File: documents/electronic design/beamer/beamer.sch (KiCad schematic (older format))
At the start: 23 parts, among them P1 CONN_01X20, P2 CONN_01X20, T1 2N7002K, T10 2N7002K, T2 2N7002K, T3 2N7002K, T4 2N7002K, T5 2N7002K, T6 2N7002K, T7 2N7002K, T8 2N7002K, T9 2N7002K, U1 NRF24L01-BRKOUT

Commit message: update schematics and pcb projects
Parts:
- T1, T10, T2, T3, T4, T5, T6, T7, T8, T9: footprint SOT23 -> 2N7002K:SOT23
- U1: footprint NRF24L01-BKKOUT -> se8r01_smd:SE8R01_SMD
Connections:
- net IR_PIN_1: now also P1.8 (P8); no longer P2.8 (P8)
- net IR_PIN_2: now also P1.9 (P9); no longer P2.7 (P7)
- net IR_PIN_3: now also P1.10 (P10); no longer P1.11 (P11)
- net IR_PIN_4: now also P1.11 (P11); no longer P1.12 (P12)
- net IR_PIN_5: now also P1.12 (P12); no longer P1.13 (P13)
- net IR_PIN_6: now also P1.13 (P13); no longer P1.14 (P14)
- net IR_PIN_7: now also P1.14 (P14); no longer P1.15 (P15)
- net IR_PIN_8: now also P1.15 (P15); no longer P1.16 (P16)
- net IR_PIN_ID: now also P1.16 (P16); no longer P1.1 (P1)
- no-connect marks 23 -> 22
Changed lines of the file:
@@
 EESchema Schematic File Version 2
+LIBS:power
+LIBS:device
+LIBS:transistors
+LIBS:conn
+LIBS:linear
+LIBS:regul
+LIBS:74xx
+LIBS:cmos4000
+LIBS:adc-dac
+LIBS:memory
+LIBS:xilinx
+LIBS:microcontrollers
+LIBS:dsp
+LIBS:microchip
+LIBS:analog_switches
+LIBS:motorola
+LIBS:texas
+LIBS:intel
+LIBS:audio
+LIBS:interface
+LIBS:digital-audio
+LIBS:philips
+LIBS:display
+LIBS:cypress
+LIBS:siliconi
+LIBS:opto
+LIBS:atmel
+LIBS:contrib
+LIBS:valves
+LIBS:2N7002K
 LIBS:NRF24L01-BRKOUT
-LIBS:ir_beamer-cache
+LIBS:conn_R
+LIBS:beamer-cache
 EELAYER 25 0
 EELAYER END
@@
 F 0 "T1" H 1150 2150 50  0000 L CNN
 F 1 "2N7002K" H 1000 2050 50  0000 L CNN
-F 2 "SOT23" H 1350 1900 50  0001 L CNN
+F 2 "2N7002K:SOT23" H 1350 1900 50  0001 L CNN
 F 3 "" H 1350 1900 60  0000 C CNN
 	1    1350 1900
@@
 F 0 "T4" H 2650 3050 50  0000 L CNN
 F 1 "2N7002K" H 2500 2950 50  0000 L CNN
-F 2 "SOT23" H 2850 2800 50  0001 L CNN
+F 2 "2N7002K:SOT23" H 2850 2800 50  0001 L CNN
 F 3 "" H 2850 2800 60  0000 C CNN
 	1    2850 2800
@@
 F 0 "T2" H 1750 2150 50  0000 L CNN
 F 1 "2N7002K" H 1600 2050 50  0000 L CNN
-F 2 "SOT23" H 1950 1900 50  0001 L CNN
+F 2 "2N7002K:SOT23" H 1950 1900 50  0001 L CNN
 F 3 "" H 1950 1900 60  0000 C CNN
 	1    1950 1900
@@
 F 0 "T3" H 2350 2150 50  0000 L CNN
 F 1 "2N7002K" H 2200 2050 50  0000 L CNN
-F 2 "SOT23" H 2550 1900 50  0001 L CNN
+F 2 "2N7002K:SOT23" H 2550 1900 50  0001 L CNN
 F 3 "" H 2550 1900 60  0000 C CNN
 	1    2550 1900
@@
 F 0 "T5" H 2950 2150 50  0000 L CNN
 F 1 "2N7002K" H 2800 2050 50  0000 L CNN
-F 2 "SOT23" H 3150 1900 50  0001 L CNN
+F 2 "2N7002K:SOT23" H 3150 1900 50  0001 L CNN
 F 3 "" H 3150 1900 60  0000 C CNN
 	1    3150 1900
@@
 F 0 "T6" H 3550 2150 50  0000 L CNN
 F 1 "2N7002K" H 3400 2050 50  0000 L CNN
-F 2 "SOT23" H 3750 1900 50  0001 L CNN
+F 2 "2N7002K:SOT23" H 3750 1900 50  0001 L CNN
 F 3 "" H 3750 1900 60  0000 C CNN
 	1    3750 1900
@@
 F 0 "T7" H 4150 2150 50  0000 L CNN
 F 1 "2N7002K" H 4000 2050 50  0000 L CNN
-F 2 "SOT23" H 4350 1900 50  0001 L CNN
+F 2 "2N7002K:SOT23" H 4350 1900 50  0001 L CNN
 F 3 "" H 4350 1900 60  0000 C CNN
 	1    4350 1900
@@
 F 0 "T8" H 4750 2150 50  0000 L CNN
 F 1 "2N7002K" H 4600 2050 50  0000 L CNN
-F 2 "SOT23" H 4950 1900 50  0001 L CNN
+F 2 "2N7002K:SOT23" H 4950 1900 50  0001 L CNN
 F 3 "" H 4950 1900 60  0000 C CNN
 	1    4950 1900
@@
 F 0 "T9" H 5350 2150 50  0000 L CNN
 F 1 "2N7002K" H 5200 2050 50  0000 L CNN
-F 2 "SOT23" H 5550 1900 50  0001 L CNN
+F 2 "2N7002K:SOT23" H 5550 1900 50  0001 L CNN
 F 3 "" H 5550 1900 60  0000 C CNN
 	1    5550 1900
@@
 F 0 "T10" H 6600 2150 50  0000 L CNN
 F 1 "2N7002K" H 6450 2050 50  0000 L CNN
-F 2 "SOT23" H 6800 1900 50  0001 L CNN
+F 2 "2N7002K:SOT23" H 6800 1900 50  0001 L CNN
 F 3 "" H 6800 1900 60  0000 C CNN
 	1    6800 1900
@@
 Text GLabel 4450 5300 0    60   Input ~ 0
 NRF_IRQ1
-Text GLabel 4450 4300 0    60   Input ~ 0
+Text GLabel 2900 4300 2    60   Input ~ 0
 IR_PIN_1
-Text GLabel 4450 4200 0    60   Input ~ 0
+Text GLabel 2900 4400 2    60   Input ~ 0
 IR_PIN_2
+Text GLabel 2900 4500 2    60   Input ~ 0
+IR_PIN_3
 Text GLabel 2900 4600 2    60   Input ~ 0
-IR_PIN_3
+IR_PIN_4
 Text GLabel 2900 4700 2    60   Input ~ 0
-IR_PIN_4
+IR_PIN_5
 Text GLabel 2900 4800 2    60   Input ~ 0
-IR_PIN_5
+IR_PIN_6
 Text GLabel 2900 4900 2    60   Input ~ 0
-IR_PIN_6
+IR_PIN_7
 Text GLabel 2900 5000 2    60   Input ~ 0
-IR_PIN_7
+IR_PIN_8
 Text GLabel 2900 5100 2    60   Input ~ 0
-IR_PIN_8
-Text GLabel 2900 3600 2    60   Input ~ 0
 IR_PIN_ID
 NoConn ~ 2800 5500
 NoConn ~ 2800 5400
 NoConn ~ 2800 5300
-NoConn ~ 2800 4500
-NoConn ~ 2800 4400
-NoConn ~ 2800 4300
 NoConn ~ 2800 4200
 NoConn ~ 2800 4100
@@
 Text GLabel 2900 5200 2    60   Input ~ 0
 PWM_38K
-NoConn ~ 4500 3650
 $Comp
 L GND #PWR05
@@
 	2800 5200 2900 5200
 Wire Wire Line
-	2800 3600 2900 3600
-Wire Wire Line
 	4050 3450 4500 3450
 Wire Wire Line
@@
 $Comp
 L NRF24L01-BRKOUT U1
-U 1 1 5713BCFC
+U 1 1 5713E8BE
 P 9200 1850
 F 0 "U1" H 8800 2450 50  0000 L CNN
 F 1 "NRF24L01-BRKOUT" H 9200 1250 50  0000 L CNN
-F 2 "NRF24L01-BKKOUT" H 9200 1850 50  0001 L CNN
+F 2 "se8r01_smd:SE8R01_SMD" H 9200 1850 50  0001 L CNN
 F 3 "" H 9200 1850 60  0000 C CNN
 	1    9200 1850
 	1    0    0    -1
 $EndComp
+Wire Wire Line
+	2800 4400 2900 4400
+Wire Wire Line
+	2800 4500 2900 4500
+NoConn ~ 4450 4300
+NoConn ~ 4450 4200
+Wire Wire Line
+	2800 4300 2900 4300
+NoConn ~ 2800 3600
 $EndSCHEMATC

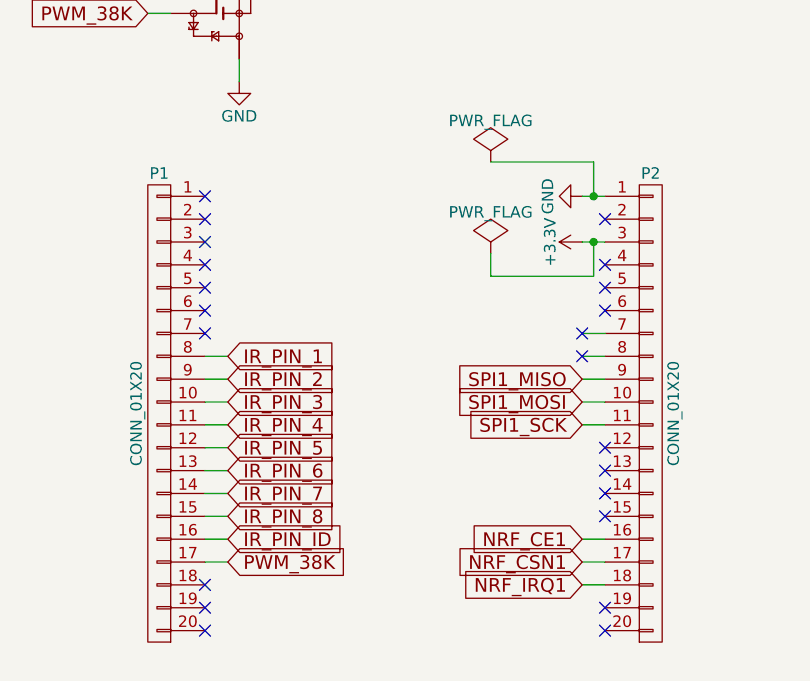
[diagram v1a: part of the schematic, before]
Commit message: finish pcb for beamer (prototype v1)
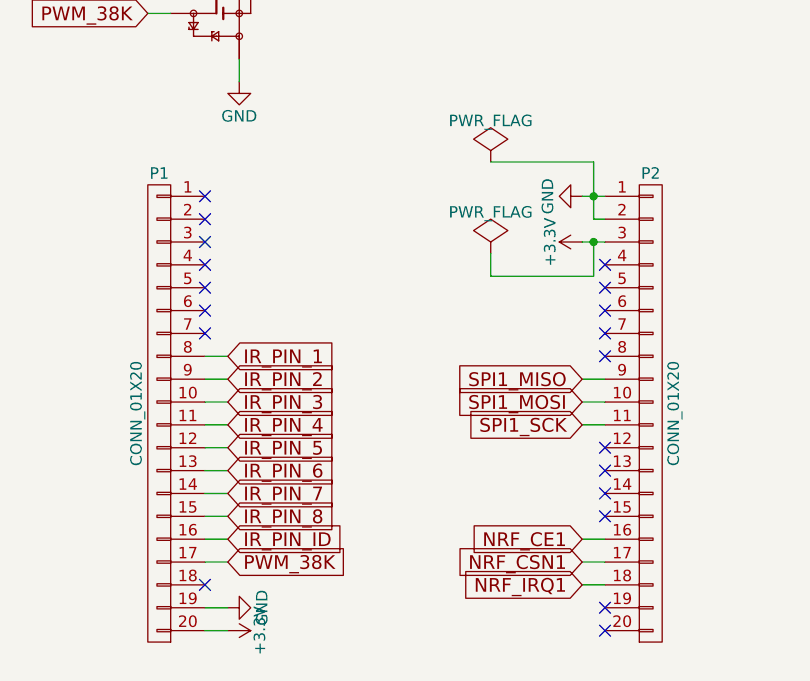
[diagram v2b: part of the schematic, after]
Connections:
- net +3V3: now also P1.20 (P20)
- net GND: now also P1.19 (P19), P2.2 (P2)
- no-connect marks 22 -> 19
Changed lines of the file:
@@
 Text GLabel 2900 5100 2    60   Input ~ 0
 IR_PIN_ID
-NoConn ~ 2800 5500
-NoConn ~ 2800 5400
 NoConn ~ 2800 5300
 NoConn ~ 2800 4200
@@
 NoConn ~ 4550 4000
 NoConn ~ 4550 3900
-NoConn ~ 4550 3700
 $Comp
 L GND #PWR03
@@
 	4450 5300 4550 5300
 Wire Wire Line
-	4450 4200 4550 4200
-Wire Wire Line
-	4450 4300 4550 4300
-Wire Wire Line
 	2800 4600 2900 4600
 Wire Wire Line
@@
 	4050 3450 4500 3450
 Wire Wire Line
-	4500 3450 4500 3600
+	4500 3450 4500 3700
 Connection ~ 4500 3600
 Wire Wire Line
@@
 Wire Wire Line
 	2800 4500 2900 4500
-NoConn ~ 4450 4300
-NoConn ~ 4450 4200
+NoConn ~ 4550 4300
+NoConn ~ 4550 4200
 Wire Wire Line
 	2800 4300 2900 4300
 NoConn ~ 2800 3600
+$Comp
+L +3.3V #PWR09
+U 1 1 57153B7B
+P 2900 5500
+F 0 "#PWR09" H 2900 5350 50  0001 C CNN
+F 1 "+3.3V" H 2900 5640 50  0000 C CNN
+F 2 "" H 2900 5500 50  0000 C CNN
+F 3 "" H 2900 5500 50  0000 C CNN
+	1    2900 5500
+	0    1    1    0
+$EndComp
+$Comp
+L GND #PWR010
+U 1 1 57153C2F
+P 2900 5400
+F 0 "#PWR010" H 2900 5150 50  0001 C CNN
+F 1 "GND" H 2900 5250 50  0000 C CNN
+F 2 "" H 2900 5400 50  0000 C CNN
+F 3 "" H 2900 5400 50  0000 C CNN
+	1    2900 5400
+	0    -1   -1   0
+$EndComp
+Wire Wire Line
+	2800 5500 2900 5500
+Wire Wire Line
+	2800 5400 2900 5400
+Wire Wire Line
+	4500 3700 4550 3700
 $EndSCHEMATC

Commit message: add capacitor to pcb
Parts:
- added C1: C, symbol C
- T1, T10, T2, T3, T4, T5, T6, T7, T8, T9: footprint 2N7002K:SOT23 -> sot23_modified:SOT23Mod
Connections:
- net +3V3: now also C1.2
- net GND: now also C1.1

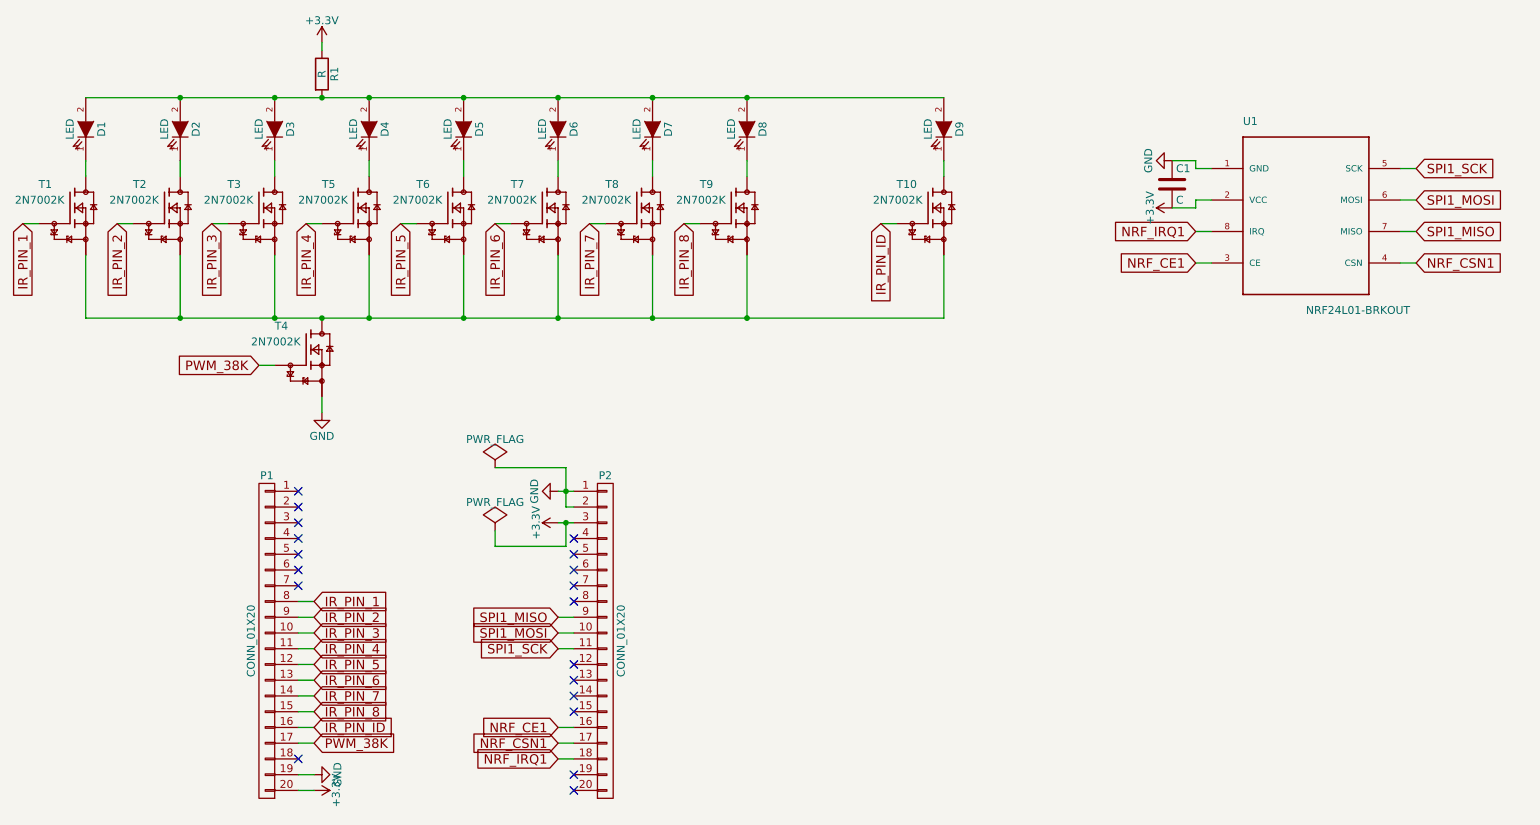
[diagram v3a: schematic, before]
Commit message: add library for shift register, update gitignore
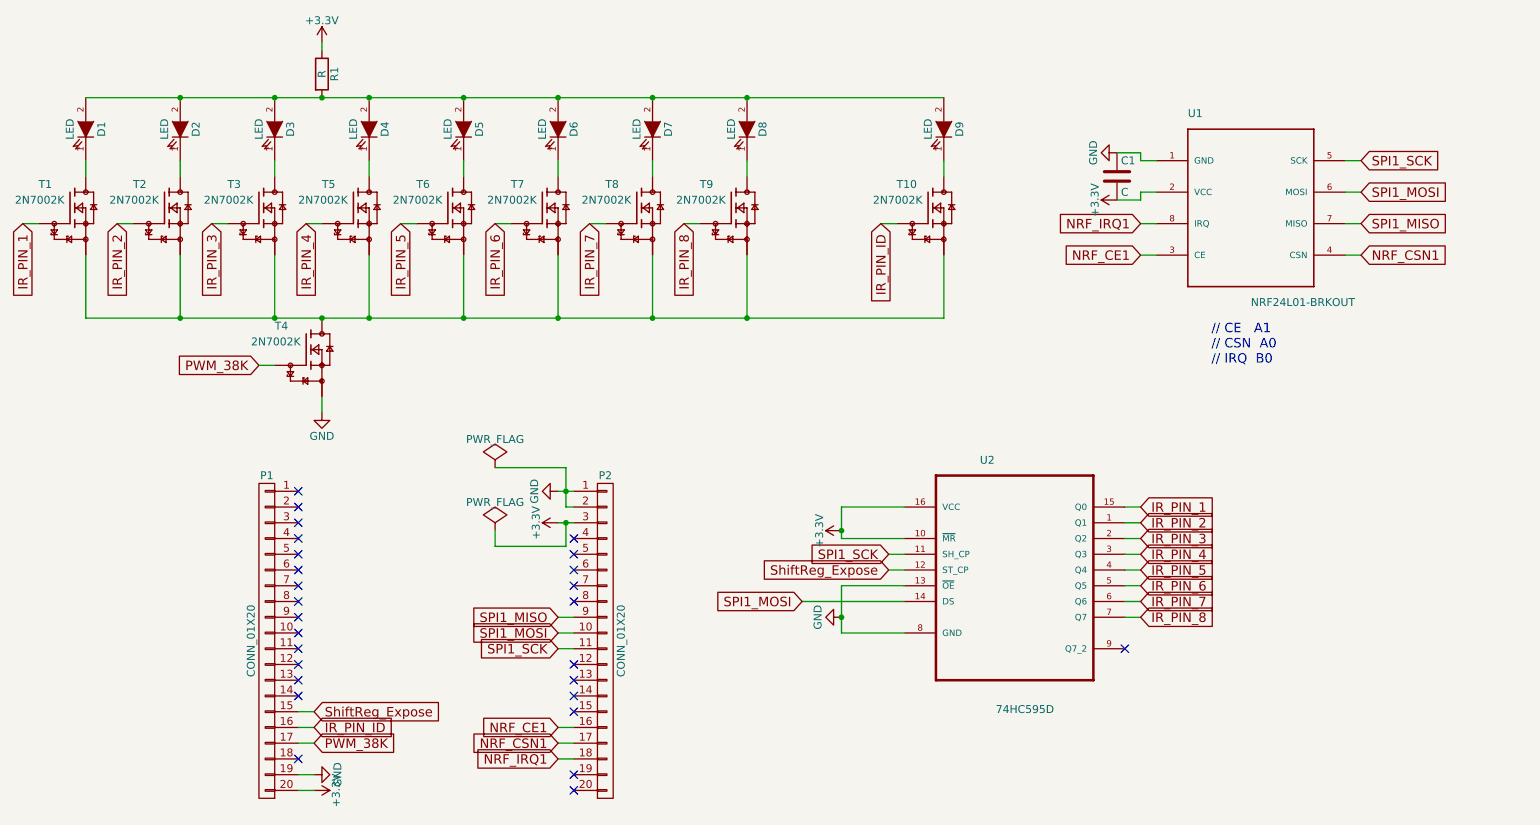
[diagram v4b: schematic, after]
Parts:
- added U2: 74HC595D, SOIC127P600X175-16N, symbol 74HC595D
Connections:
- net +3V3: now also U2.10 (~MR), U2.16 (VCC)
- net GND: now also U2.13 (~OE), U2.8 (GND)
- net IR_PIN_1: now also U2.15 (Q0); no longer P1.8 (P8)
- net IR_PIN_2: now also U2.1 (Q1); no longer P1.9 (P9)
- net IR_PIN_3: now also U2.2 (Q2); no longer P1.10 (P10)
- net IR_PIN_4: now also U2.3 (Q3); no longer P1.11 (P11)
- net IR_PIN_5: now also U2.4 (Q4); no longer P1.12 (P12)
- net IR_PIN_6: now also U2.5 (Q5); no longer P1.13 (P13)
- net IR_PIN_7: now also U2.6 (Q6); no longer P1.14 (P14)
- net IR_PIN_8: now also U2.7 (Q7); no longer P1.15 (P15)
- net SPI1_MOSI: now also U2.14 (DS)
- net SPI1_SCK: now also U2.11 (SH_CP)
- new net ShiftReg_Expose: P1.15 (P15), U2.12 (ST_CP)
- no-connect marks 19 -> 27
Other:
- note added: "// CE A1\n// CSN A0\n// IRQ B0"
- moved on the sheet: C1, U1
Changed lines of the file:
@@
 LIBS:valves
 LIBS:NRF24L01-BRKOUT
+LIBS:conn_R
 LIBS:2N7002K
+LIBS:74HC595D
+LIBS:beamer-cache
 EELAYER 25 0
 EELAYER END
@@
 	1    0    0    -1
 $EndComp
-Text GLabel 9900 1750 2    60   Input ~ 0
+Text GLabel 9550 1700 2    60   Input ~ 0
 SPI1_MOSI
-Text GLabel 9900 1950 2    60   Input ~ 0
+Text GLabel 9550 1900 2    60   Input ~ 0
 SPI1_MISO
-Text GLabel 9900 2150 2    60   Input ~ 0
+Text GLabel 9550 2100 2    60   Input ~ 0
 NRF_CSN1
-Text GLabel 8500 1950 0    60   Input ~ 0
+Text GLabel 8150 1900 0    60   Input ~ 0
 NRF_IRQ1
-Text GLabel 8500 2150 0    60   Input ~ 0
+Text GLabel 8150 2100 0    60   Input ~ 0
 NRF_CE1
-Text GLabel 9900 1550 2    60   Input ~ 0
+Text GLabel 9550 1500 2    60   Input ~ 0
 SPI1_SCK
 $Comp
@@
 Text GLabel 4450 5300 0    60   Input ~ 0
 NRF_IRQ1
-Text GLabel 2900 4300 2    60   Input ~ 0
+Text GLabel 8150 3700 2    60   Input ~ 0
 IR_PIN_1
-Text GLabel 2900 4400 2    60   Input ~ 0
+Text GLabel 8150 3800 2    60   Input ~ 0
 IR_PIN_2
-Text GLabel 2900 4500 2    60   Input ~ 0
+Text GLabel 8150 3900 2    60   Input ~ 0
 IR_PIN_3
-Text GLabel 2900 4600 2    60   Input ~ 0
+Text GLabel 8150 4000 2    60   Input ~ 0
 IR_PIN_4
-Text GLabel 2900 4700 2    60   Input ~ 0
+Text GLabel 8150 4100 2    60   Input ~ 0
 IR_PIN_5
-Text GLabel 2900 4800 2    60   Input ~ 0
+Text GLabel 8150 4200 2    60   Input ~ 0
 IR_PIN_6
-Text GLabel 2900 4900 2    60   Input ~ 0
+Text GLabel 8150 4300 2    60   Input ~ 0
 IR_PIN_7
-Text GLabel 2900 5000 2    60   Input ~ 0
+Text GLabel 8150 4400 2    60   Input ~ 0
 IR_PIN_8
 Text GLabel 2900 5100 2    60   Input ~ 0
@@
 L GND #PWR05
 U 1 1 57142C4E
-P 8350 1500
-F 0 "#PWR05" H 8350 1250 50  0001 C CNN
-F 1 "GND" H 8350 1350 50  0000 C CNN
-F 2 "" H 8350 1500 50  0000 C CNN
-F 3 "" H 8350 1500 50  0000 C CNN
-	1    8350 1500
+P 8000 1450
+F 0 "#PWR05" H 8000 1200 50  0001 C CNN
+F 1 "GND" H 8000 1300 50  0000 C CNN
+F 2 "" H 8000 1450 50  0000 C CNN
+F 3 "" H 8000 1450 50  0000 C CNN
+	1    8000 1450
 	0    1    1    0
 $EndComp
@@
 L +3.3V #PWR06
 U 1 1 57142CA4
-P 8350 1800
-F 0 "#PWR06" H 8350 1650 50  0001 C CNN
-F 1 "+3.3V" H 8350 1940 50  0000 C CNN
-F 2 "" H 8350 1800 50  0000 C CNN
-F 3 "" H 8350 1800 50  0000 C CNN
-	1    8350 1800
+P 8000 1750
+F 0 "#PWR06" H 8000 1600 50  0001 C CNN
+F 1 "+3.3V" H 8000 1890 50  0000 C CNN
+F 2 "" H 8000 1750 50  0000 C CNN
+F 3 "" H 8000 1750 50  0000 C CNN
+	1    8000 1750
 	0    -1   -1   0
 $EndComp
@@
 L NRF24L01-BRKOUT U1
 U 1 1 5713E8BE
-P 9200 1850
-F 0 "U1" H 8800 2450 50  0000 L CNN
-F 1 "NRF24L01-BRKOUT" H 9200 1250 50  0000 L CNN
-F 2 "se8r01_smd:SE8R01_SMD" H 9200 1850 50  0001 L CNN
-F 3 "" H 9200 1850 60  0000 C CNN
-	1    9200 1850
+P 8850 1800
+F 0 "U1" H 8450 2400 50  0000 L CNN
+F 1 "NRF24L01-BRKOUT" H 8850 1200 50  0000 L CNN
+F 2 "se8r01_smd:SE8R01_SMD" H 8850 1800 50  0001 L CNN
+F 3 "" H 8850 1800 60  0000 C CNN
+	1    8850 1800
 	1    0    0    -1
 $EndComp
@@
 L C C1
 U 1 1 57177FF4
-P 8350 1650
-F 0 "C1" H 8375 1750 50  0000 L CNN
-F 1 "C" H 8375 1550 50  0000 L CNN
-F 2 "" H 8388 1500 50  0000 C CNN
-F 3 "" H 8350 1650 50  0000 C CNN
-	1    8350 1650
-	1    0    0    -1
-$EndComp
-$Comp
-L PWR_FLAG #FLG07
+P 8000 1600
+F 0 "C1" H 8025 1700 50  0000 L CNN
+F 1 "C" H 8025 1500 50  0000 L CNN
+F 2 "" H 8038 1450 50  0000 C CNN
+F 3 "" H 8000 1600 50  0000 C CNN
+	1    8000 1600
+	1    0    0    -1
+$EndComp
+$Comp
+L PWR_FLAG #FLG09
 U 1 1 57142E4E
 P 4050 3450
-F 0 "#FLG07" H 4050 3545 50  0001 C CNN
+F 0 "#FLG09" H 4050 3545 50  0001 C CNN
 F 1 "PWR_FLAG" H 4050 3630 50  0000 C CNN
 F 2 "" H 4050 3450 50  0000 C CNN
@@
 $EndComp
 $Comp
-L PWR_FLAG #FLG08
+L PWR_FLAG #FLG010
 U 1 1 57142EAB
 P 4050 3850
-F 0 "#FLG08" H 4050 3945 50  0001 C CNN
+F 0 "#FLG010" H 4050 3945 50  0001 C CNN
 F 1 "PWR_FLAG" H 4050 4030 50  0000 C CNN
 F 2 "" H 4050 3850 50  0000 C CNN
@@
 	1    0    0    -1
 $EndComp
+Text Notes 8600 2800 0    60   ~ 0
+// CE   A1\n// CSN  A0\n// IRQ  B0
+$Comp
+L 74HC595D U2
+U 1 1 57630FAB
+P 7350 4000
+F 0 "U2" H 7129 4598 50  0000 L CNN
+F 1 "74HC595D" H 7230 3015 50  0000 L CNN
+F 2 "SOIC127P600X175-16N" H 7350 4000 50  0001 L CNN
+F 3 "" H 7350 4000 60  0000 C CNN
+	1    7350 4000
+	1    0    0    -1
+$EndComp
+$Comp
+L GND #PWR011
+U 1 1 5763139E
+P 6250 4400
+F 0 "#PWR011" H 6250 4150 50  0001 C CNN
+F 1 "GND" H 6250 4250 50  0000 C CNN
+F 2 "" H 6250 4400 50  0000 C CNN
+F 3 "" H 6250 4400 50  0000 C CNN
+	1    6250 4400
+	0    1    1    0
+$EndComp
+$Comp
+L +3.3V #PWR012
+U 1 1 576314B2
+P 6250 3850
+F 0 "#PWR012" H 6250 3700 50  0001 C CNN
+F 1 "+3.3V" H 6250 3990 50  0000 C CNN
+F 2 "" H 6250 3850 50  0000 C CNN
+F 3 "" H 6250 3850 50  0000 C CNN
+	1    6250 3850
+	0    -1   -1   0
+$EndComp
 Wire Wire Line
 	4050 3450 4500 3450
@@
 	4050 3850 4050 3950
 Wire Wire Line
-	8500 1800 8350 1800
-Wire Wire Line
-	8500 1750 8500 1800
-Wire Wire Line
-	8600 1750 8500 1750
-Wire Wire Line
-	8500 1500 8350 1500
-Wire Wire Line
-	8500 1550 8500 1500
-Wire Wire Line
-	8600 1550 8500 1550
+	8150 1750 8000 1750
+Wire Wire Line
+	8150 1700 8150 1750
+Wire Wire Line
+	8250 1700 8150 1700
+Wire Wire Line
+	8150 1450 8000 1450
+Wire Wire Line
+	8150 1500 8150 1450
+Wire Wire Line
+	8250 1500 8150 1500
 Wire Wire Line
 	4500 3700 4550 3700
@@
 	2800 5500 2900 5500
 Wire Wire Line
-	2800 4300 2900 4300
-Wire Wire Line
-	2800 4500 2900 4500
-Wire Wire Line
-	2800 4400 2900 4400
+	8050 3700 8150 3700
+Wire Wire Line
+	8050 3900 8150 3900
+Wire Wire Line
+	8050 3800 8150 3800
 Connection ~ 4500 3800
 Connection ~ 4500 3600
@@
 	2800 5100 2900 5100
 Wire Wire Line
-	2800 5000 2900 5000
-Wire Wire Line
-	2800 4900 2900 4900
-Wire Wire Line
-	2800 4800 2900 4800
-Wire Wire Line
-	2800 4700 2900 4700
-Wire Wire Line
-	2800 4600 2900 4600
+	8050 4400 8150 4400
+Wire Wire Line
+	8050 4300 8150 4300
+Wire Wire Line
+	8050 4200 8150 4200
+Wire Wire Line
+	8050 4100 8150 4100
+Wire Wire Line
+	8050 4000 8150 4000
 Wire Wire Line
 	4450 5300 4550 5300
@@
 	1450 1600 1450 1500
 Wire Wire Line
-	8600 1950 8500 1950
-Wire Wire Line
-	8600 2150 8500 2150
-Wire Wire Line
-	9800 2150 9900 2150
-Wire Wire Line
-	9800 1950 9900 1950
-Wire Wire Line
-	9800 1750 9900 1750
-Wire Wire Line
-	9800 1550 9900 1550
+	8250 1900 8150 1900
+Wire Wire Line
+	8250 2100 8150 2100
+Wire Wire Line
+	9450 2100 9550 2100
+Wire Wire Line
+	9450 1900 9550 1900
+Wire Wire Line
+	9450 1700 9550 1700
+Wire Wire Line
+	9450 1500 9550 1500
+Wire Wire Line
+	6650 3700 6250 3700
+Wire Wire Line
+	6250 3700 6250 3900
+Wire Wire Line
+	6250 3900 6650 3900
+Connection ~ 6250 3850
+Wire Wire Line
+	6250 4500 6650 4500
+Wire Wire Line
+	6250 4200 6250 4500
+Wire Wire Line
+	6650 4200 6250 4200
+Connection ~ 6250 4400
+NoConn ~ 8050 4600
+Text GLabel 6550 4000 0    60   Input ~ 0
+SPI1_SCK
+Text GLabel 6000 4300 0    60   Input ~ 0
+SPI1_MOSI
+Wire Wire Line
+	6000 4300 6650 4300
+Wire Wire Line
+	6550 4000 6650 4000
+Text GLabel 2900 5000 2    60   Input ~ 0
+ShiftReg_Expose
+Text GLabel 6550 4100 0    60   Input ~ 0
+ShiftReg_Expose
+Wire Wire Line
+	6550 4100 6650 4100
+Wire Wire Line
+	2900 5000 2800 5000
+NoConn ~ 2800 4900
+NoConn ~ 2800 4800
+NoConn ~ 2800 4700
+NoConn ~ 2800 4600
+NoConn ~ 2800 4500
+NoConn ~ 2800 4400
+NoConn ~ 2800 4300
 $EndSCHEMATC
